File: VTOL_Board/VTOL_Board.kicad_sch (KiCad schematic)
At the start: 19 parts, among them J101 MOTOR, J102 ENCODER, Q101 MMBT3904, Q102 MMBT3906

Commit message: Modify boilerplate for vtol
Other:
- title: Inverted Pendulum Controller -> VTOL Board
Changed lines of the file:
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@@
   (paper "A4")
   (title_block
-    (title "Inverted Pendulum Controller")
+    (title "VTOL Board")
     (date "${ISSUE}")
     (rev "${REVISION}")

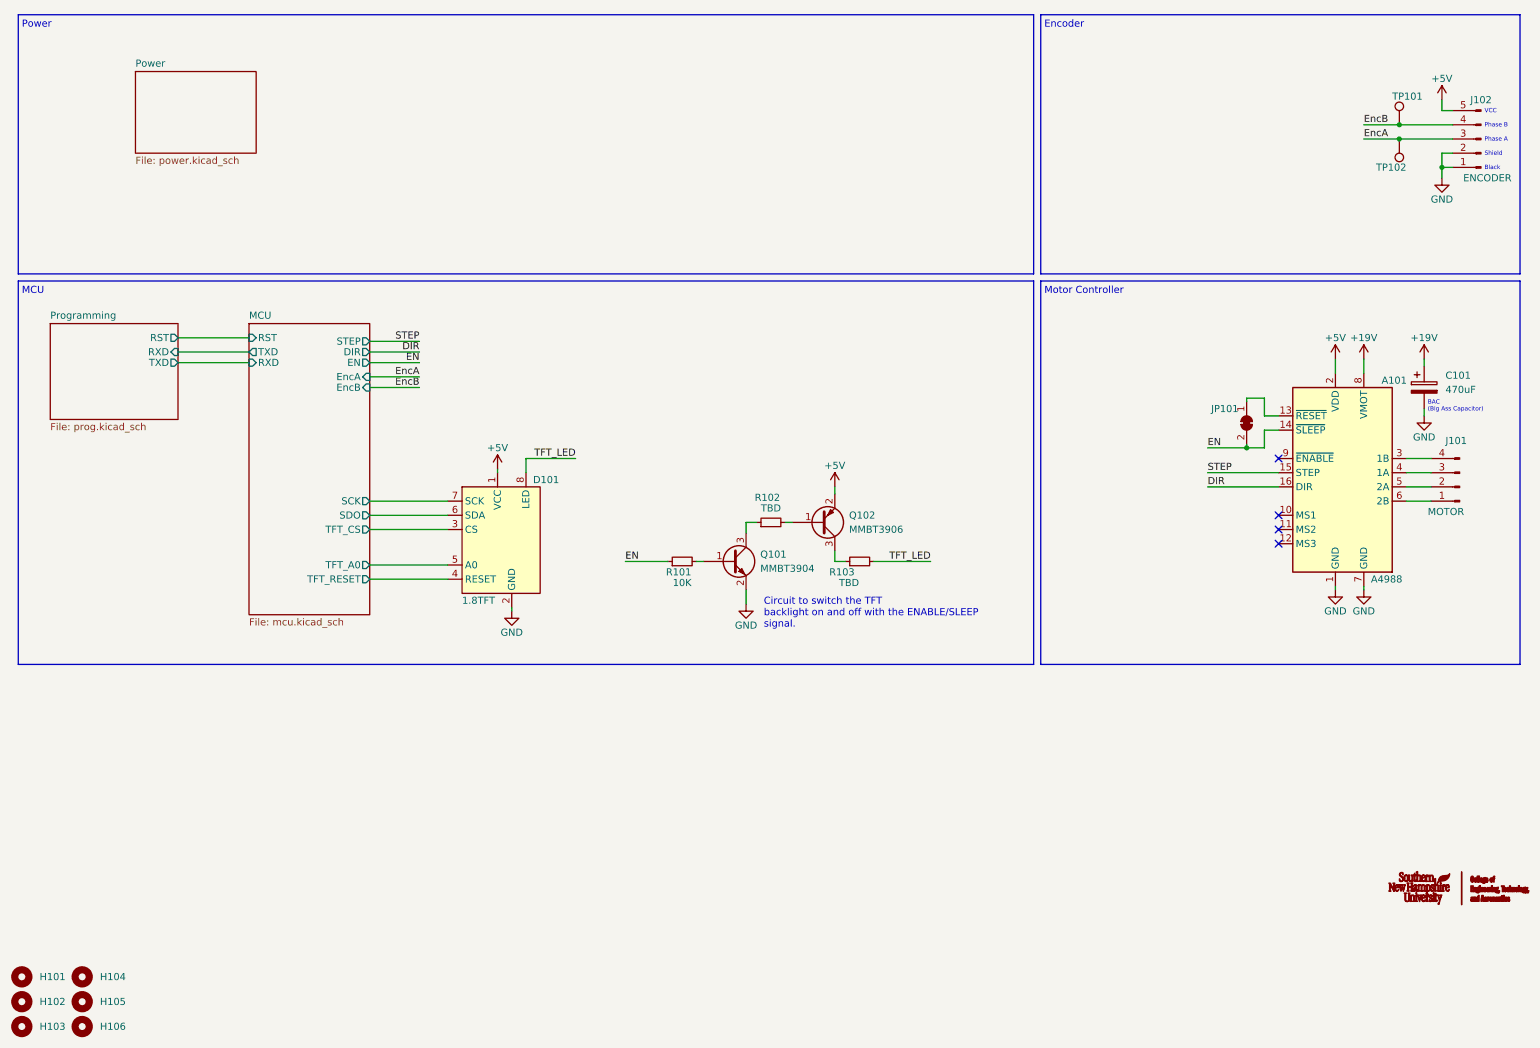
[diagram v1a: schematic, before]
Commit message: Use small hirose connectors
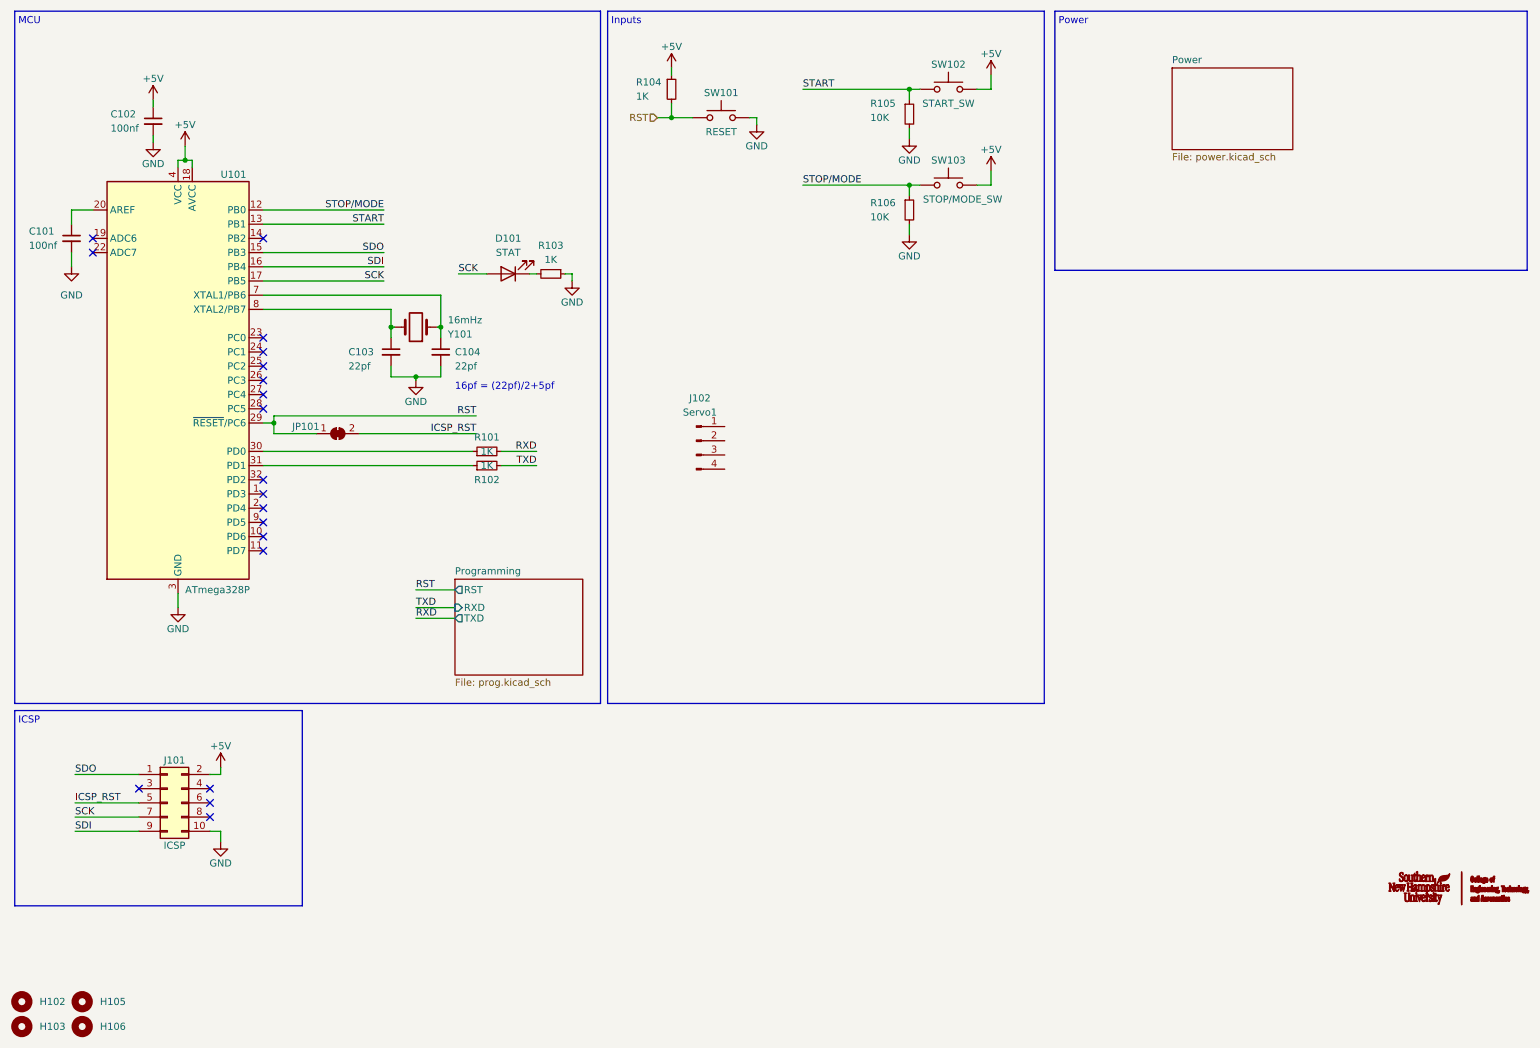
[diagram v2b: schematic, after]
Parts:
- removed A101: A4988, Module:Pololu_Breakout-16_15.2x20.3mm, symbol Driver_Motor:Pololu_Breakout_A4988
- removed C101: 470uF, Capacitor_THT:CP_Radial_D10.0mm_P3.80mm, symbol Device:C_Polarized
- removed D101: 1.8TFT, Connector_JST:JST_EH_B8B-EH-A_1x08_P2.50mm_Vertical, symbol KenwoodFox:1.8TFT
- removed H101, H104: PiMountingHole, MountingHole:MountingHole_2.7mm, symbol Mechanical:MountingHole
- removed J101: MOTOR, Connector_JST:JST_EH_B4B-EH-A_1x04_P2.50mm_Vertical, symbol Connector:Conn_01x04_Male
- removed J102: ENCODER, Connector_JST:JST_EH_B5B-EH-A_1x05_P2.50mm_Vertical, symbol Connector:Conn_01x05_Male
- removed Q101: MMBT3904, Package_TO_SOT_SMD:SOT-23, symbol Transistor_BJT:MMBT3904
- removed Q102: MMBT3906, Package_TO_SOT_SMD:SOT-23, symbol Transistor_BJT:MMBT3906
- removed TP101, TP102: TestPoint, TestPoint:TestPoint_Pad_1.5x1.5mm, symbol Connector:TestPoint
- added C101, C102: 100nf, Capacitor_SMD:C_0805_2012Metric, symbol Device:C_Small
- added C103, C104: 22pf, Capacitor_SMD:C_0805_2012Metric, symbol Device:C_Small
- added D101: STAT, LED_SMD:LED_0805_2012Metric, symbol Device:LED
- added J101: ICSP, Connector:Tag-Connect_TC2050-IDC-FP_2x05_P1.27mm_Vertical, symbol Connector_Generic:Conn_02x05_Odd_Even
- added J102: Servo1, Connector_Hirose:Hirose_DF13-04P-1.25DS_1x04_P1.25mm_Horizontal, symbol Connector:Conn_01x04_Male
- added R104: 1K, Resistor_SMD:R_0805_2012Metric, symbol Device:R_Small
- added R105, R106: 10K, Resistor_SMD:R_0805_2012Metric, symbol Device:R_Small
- added SW101: RESET, Button_Switch_THT:SW_PUSH_6mm_H5mm, symbol Switch:SW_Push
- added SW102: START_SW, Button_Switch_THT:SW_PUSH_6mm_H5mm, symbol Switch:SW_Push
- added SW103: STOP/MODE_SW, Button_Switch_THT:SW_PUSH_6mm_H5mm, symbol Switch:SW_Push
- added U101: ATmega328P, Package_QFP:TQFP-32_7x7mm_P0.8mm, symbol MCU_Microchip_ATmega:ATmega328P-A
- added Y101: 16mHz, Crystal:Crystal_SMD_HC49-SD, symbol Device:Crystal
- JP101: value SolderJumper_2_Bridged -> RSTBridge; footprint Jumper:SolderJumper-2_P1.3mm_Bridged2Bar_Pad1.0x1.5mm -> Jumper:SolderJumper-2_P1.3mm_Bridged_Pad1.0x1.5mm
- R101: value 10K -> 1K
- R102, R103: value TBD -> 1K
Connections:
- net +5V: now also C102.1, J101.2 (Pin_2), R104.1, SW102.2, SW103.2, U101.18 (AVCC), U101.4 (VCC), U101.6 (VCC)
- net GND: now also R103.1, C101.2, C102.2, C103.2, C104.2, J101.10 (Pin_10), R105.2, R106.2, SW101.2, U101.21 (GND), U101.3 (GND), U101.5 (GND)
- net RXD: now reaches R101.2
- net at R102.1: now also U101.31 (PD1)
- net RST: now reaches JP101.1 (A)
- net RST: now also R104.2, SW101.1, U101.29 (~{RESET}/PC6)
- net TXD: now reaches R102.2
- net EN: no longer names the net of R101.1
- net EN: now also U101.30 (PD0); no longer JP101.2 (B)
- net TFT_LED: no longer names the net of R103.2
- net TFT_LED: now also D101.1 (K)
- new net: C101.1, U101.20 (AREF)
- new net: C103.1, U101.8 (XTAL2/PB7), Y101.2
- new net: C104.1, U101.7 (XTAL1/PB6), Y101.1
- new net ICSP_RST: J101.5 (Pin_5), JP101.2 (B)
- new net SCK: D101.2 (A), J101.7 (Pin_7), U101.17 (PB5)
- new net SDI: J101.9 (Pin_9), U101.16 (PB4)
- new net SDO: J101.1 (Pin_1), U101.15 (PB3)
- new net START: R105.1, SW102.1, U101.13 (PB1)
- new net STOP/MODE: R106.1, SW103.1, U101.12 (PB0)
- no-connect marks 4 -> 19
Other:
- removed sheet MCU
- note added: "16pf = (22pf)/2+5pf"
- note added: "ICSP"
- note added: "Inputs"
- note removed: "BAC (Big Ass Capacitor)"
- note removed: "Black"
- note removed: "Circuit to switch the TFT backlight on and off with the ENABLE/SLEEP signal."
- note removed: "Encoder"
- note removed: "Motor Controller"
- note removed: "Phase A"
- note removed: "Phase B"
- note removed: "Shield"
- note removed: "VCC"
